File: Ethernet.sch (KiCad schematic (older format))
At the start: 11 parts

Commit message: Up
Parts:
- added U?: 93LC46, symbol 93LC46
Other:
- moved on the sheet: C?, R?, U?, Y?

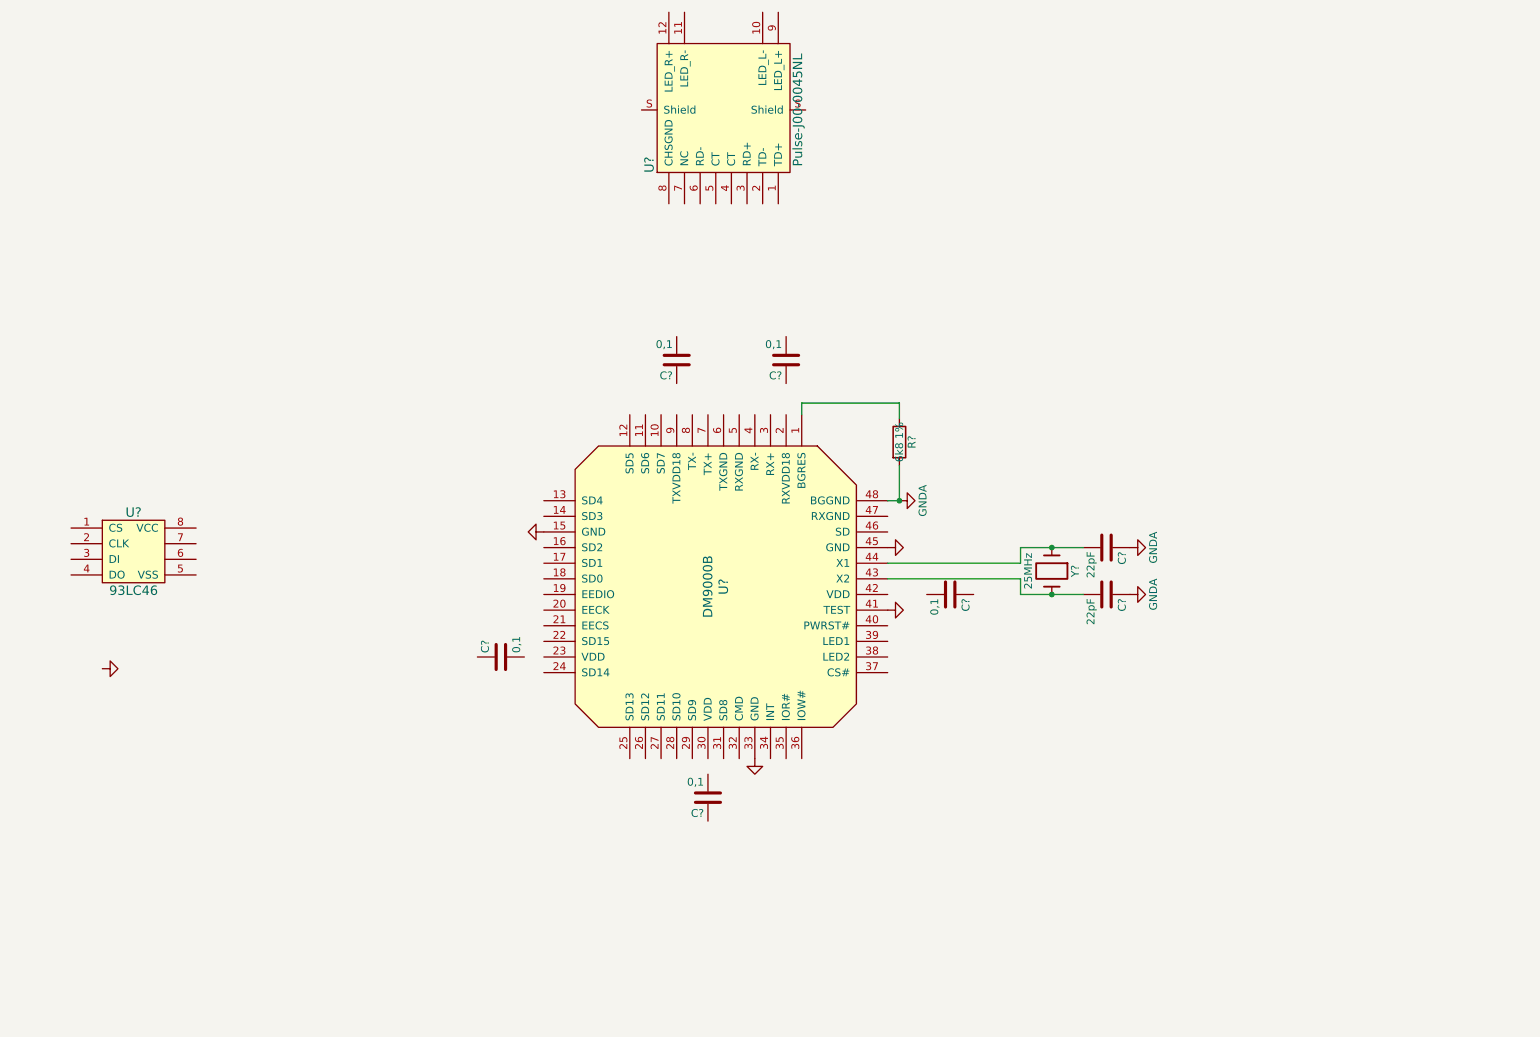
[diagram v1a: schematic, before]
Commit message: Pulse jack added
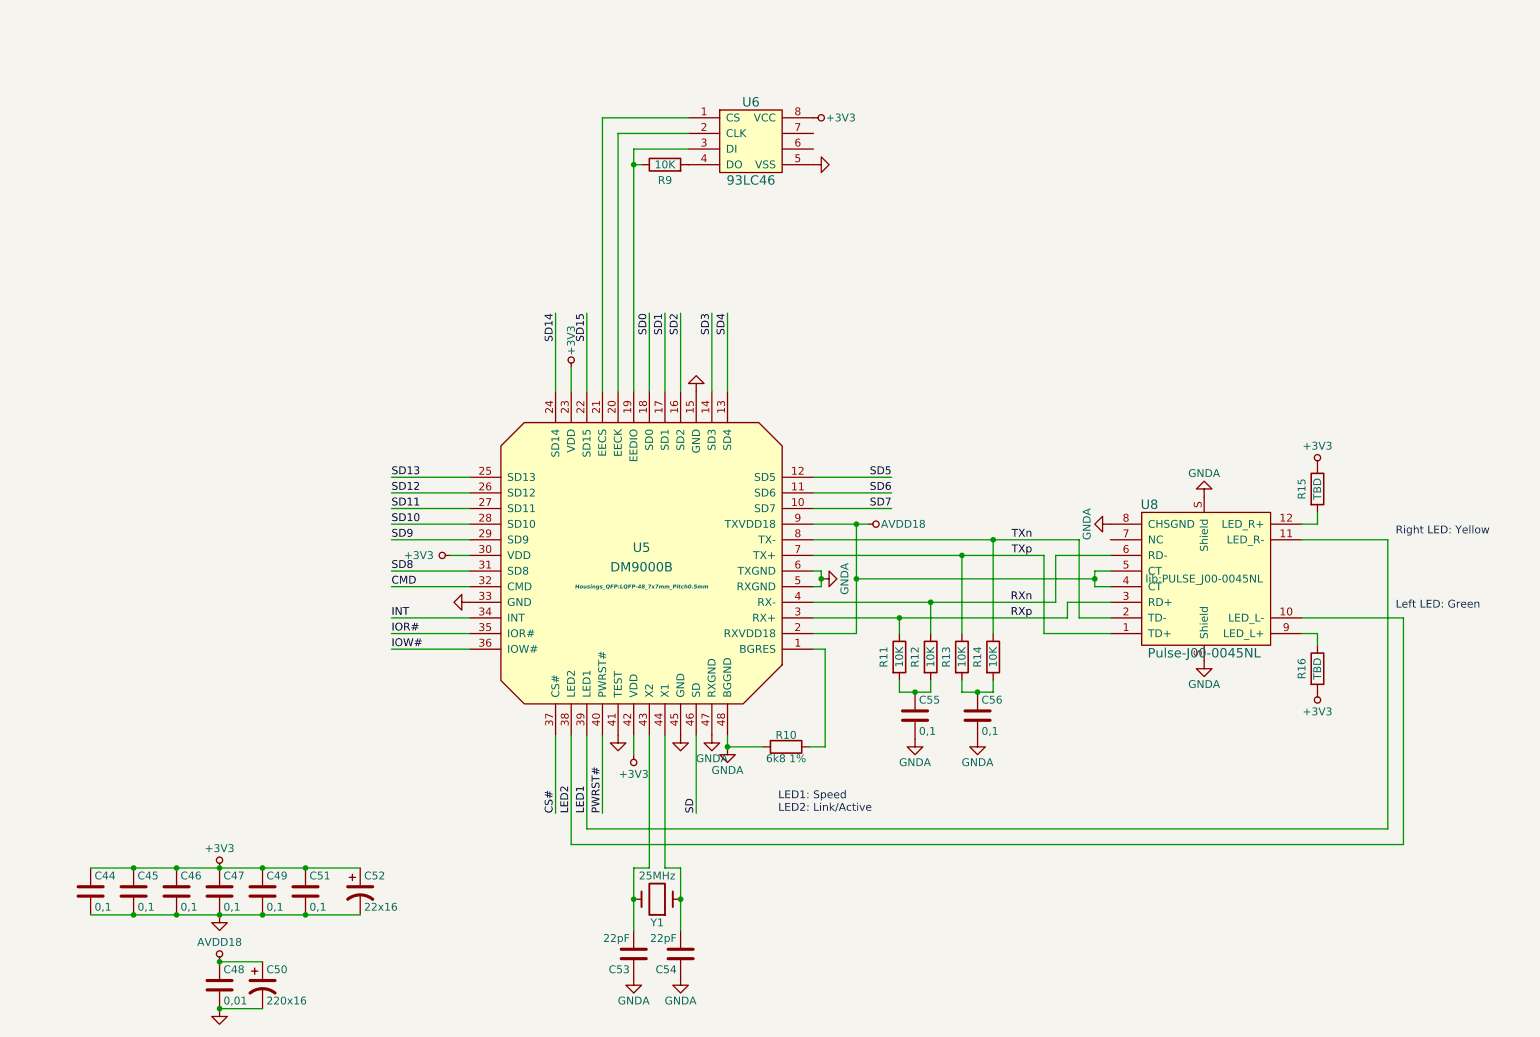
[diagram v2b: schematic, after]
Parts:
- added C44, C55, C56: 0,1, symbol C
- added C48: 0,01, symbol C
- added C50: 220x16, symbol CP1
- added C52: 22x16, symbol CP1
- added R11, R12, R13, R14, R9: 10K, symbol R
- added R15, R16: TBD, symbol R
- U5: renamed from U?; footprint (none) -> Housings_QFP:LQFP-48_7x7mm_Pitch0.5mm
- U8: renamed from U?; footprint (none) -> lib:PULSE_J00-0045NL
- gave numbers to parts that had none: 10
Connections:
- net GND: now also C45.2, C46.2, C47.2, C49.2, C51.2, U6.5 (VSS), C44.2, C48.2, C50.2, C52.2
- net GNDA: now also U5.47 (RXGND), U5.5 (RXGND), U5.6 (TXGND), U8.8 (CHSGND), U8.S (Shield), C55.2, C56.2
- net SD7: now reaches U5.10 (SD7)
- net SD6: now reaches U5.11 (SD6)
- net SD5: now reaches U5.12 (SD5)
- net SD4: now reaches U5.13 (SD4)
- net SD3: now reaches U5.14 (SD3)
- net SD2: now reaches U5.16 (SD2)
- net SD1: now reaches U5.17 (SD1)
- net SD0: now reaches U5.18 (SD0)
- net at U5.19 (EEDIO): now also U6.3 (DI), R9.1
- net AVDD18: now reaches U5.2 (RXVDD18)
- net AVDD18: now also U5.9 (TXVDD18), U8.4 (CT), U8.5 (CT), C48.1, C50.1
- net at U5.20 (EECK): now also U6.2 (CLK)
- net at U5.21 (EECS): now also U6.1 (CS)
- net SD15: now reaches U5.22 (SD15)
- net +3V3: now reaches U5.23 (VDD)
- net +3V3: now also C45.1, C46.1, C47.1, C49.1, C51.1, U5.30 (VDD), U5.42 (VDD), U6.8 (VCC), C44.1, C52.1, R15.1, R16.2
- net SD14: now reaches U5.24 (SD14)
- net SD13: now reaches U5.25 (SD13)
- net SD12: now reaches U5.26 (SD12)
- net SD11: now reaches U5.27 (SD11)
- net SD10: now reaches U5.28 (SD10)
- net SD9: now reaches U5.29 (SD9)
- net RXp: now reaches U5.3 (RX+)
- net RXp: now also U8.3 (RD+), R11.1
- net SD8: now reaches U5.31 (SD8)
- net CMD: now reaches U5.32 (CMD)
- net INT: now reaches U5.34 (INT)
- net IOR#: now reaches U5.35 (IOR#)
- net IOW#: now reaches U5.36 (IOW#)
- net CS#: now reaches U5.37 (CS#)
- net LED2: now reaches U5.38 (LED2)
- net LED2: now also U8.10 (LED_L-)
- net LED1: now reaches U5.39 (LED1)
- net LED1: now also U8.11 (LED_R-)
- net RXn: now reaches U5.4 (RX-)
- net RXn: now also U8.6 (RD-), R12.1
- net PWRST#: now reaches U5.40 (PWRST#)
- net SD: now reaches U5.46 (SD)
- net TXp: now reaches U5.7 (TX+)
- net TXp: now also U8.1 (TD+), R13.1
- net TXn: now reaches U5.8 (TX-)
- net TXn: now also U8.2 (TD-), R14.1
- net at U8.12 (LED_R+): now also R15.2
- net at U8.9 (LED_L+): now also R16.1
- net at U6.4 (DO): now also R9.2
- new net: C55.1, R11.2, R12.2
- new net: C56.1, R13.2, R14.2
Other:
- note added: "LED1: Speed\nLED2: Link/Active"
- note added: "Left LED: Green"
- note added: "Right LED: Yellow"
- moved on the sheet: C45, C46, C47, C49, C51, C53, C54, R10, U5, U6, U8, Y1

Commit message: Update
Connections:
- net SD: no longer names the net of U5.46 (SD)
- no-connect marks 0 -> 2
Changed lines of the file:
@@
 Wire Wire Line
 	6100 4125 6600 4125
-Text Label 4450 2875 3    50   ~ 0
+Text Label 2500 3050 2    50   ~ 0
 SD14
 Wire Wire Line
-	4450 3375 4450 2875
+	2000 3050 2500 3050
 Text Label 4650 2875 3    50   ~ 0
 SD15
@@
 Text Label 4750 6075 1    50   ~ 0
 PWRST#
-Wire Wire Line
-	5350 5575 5350 6075
-Text Label 5350 6075 1    50   ~ 0
-SD
 $Comp
 L GNDA #PWR0105
@@
 	-1   0    0    1
 $EndComp
+NoConn ~ 8000 4325
+Text HLabel 1775 1100 0    60   BiDi ~ 0
+ETH_SD[0:15]
+Wire Bus Line
+	1775 1100 1900 1100
+Wire Bus Line
+	1900 1100 1900 3050
+Text Label 2500 2950 2    50   ~ 0
+SD13
+Wire Wire Line
+	2000 2850 2500 2850
+Wire Wire Line
+	2000 2650 2500 2650
+Wire Wire Line
+	2000 2550 2500 2550
+Text Label 2500 2850 2    50   ~ 0
+SD12
+Text Label 2500 2750 2    50   ~ 0
+SD11
+Text Label 2500 2650 2    50   ~ 0
+SD10
+Text Label 2500 2550 2    50   ~ 0
+SD9
+Wire Wire Line
+	2000 2750 2500 2750
+Wire Wire Line
+	2000 2950 2500 2950
+Entry Wire Line
+	1900 1550 2000 1650
+Entry Wire Line
+	1900 1650 2000 1750
+Entry Wire Line
+	1900 1750 2000 1850
+Entry Wire Line
+	1900 1850 2000 1950
+Entry Wire Line
+	1900 1950 2000 2050
+Entry Wire Line
+	1900 2050 2000 2150
+Entry Wire Line
+	1900 2150 2000 2250
+Entry Wire Line
+	1900 2250 2000 2350
+Entry Wire Line
+	1900 2350 2000 2450
+Entry Wire Line
+	1900 2450 2000 2550
+Entry Wire Line
+	1900 2550 2000 2650
+Entry Wire Line
+	1900 2650 2000 2750
+Entry Wire Line
+	1900 2750 2000 2850
+Entry Wire Line
+	1900 2850 2000 2950
+Entry Wire Line
+	1900 2950 2000 3050
+Entry Wire Line
+	1900 3050 2000 3150
+Text Label 2500 1650 2    50   ~ 0
+SD0
+Wire Wire Line
+	2000 1650 2500 1650
+Text Label 2500 1750 2    50   ~ 0
+SD1
+Wire Wire Line
+	2000 1750 2500 1750
+Text Label 2500 1850 2    50   ~ 0
+SD2
+Wire Wire Line
+	2000 1850 2500 1850
+Text Label 2500 1950 2    50   ~ 0
+SD3
+Wire Wire Line
+	2000 1950 2500 1950
+Text Label 2500 2050 2    50   ~ 0
+SD4
+Wire Wire Line
+	2000 2050 2500 2050
+Text Label 2500 2350 2    50   ~ 0
+SD7
+Wire Wire Line
+	2000 2250 2500 2250
+Text Label 2500 2250 2    50   ~ 0
+SD6
+Text Label 2500 2150 2    50   ~ 0
+SD5
+Wire Wire Line
+	2000 2150 2500 2150
+Wire Wire Line
+	2000 2350 2500 2350
+Wire Wire Line
+	2000 2450 2500 2450
+Text Label 2500 2450 2    50   ~ 0
+SD8
+Text Label 2500 3150 2    50   ~ 0
+SD15
+Wire Wire Line
+	2000 3150 2500 3150
+Text Label 4450 2875 3    50   ~ 0
+SD14
+Wire Wire Line
+	4450 3375 4450 2875
+Wire Wire Line
+	1775 4000 2275 4000
+Text Label 2275 4000 2    50   ~ 0
+CMD
+Wire Wire Line
+	1775 4200 2275 4200
+Text Label 2275 4200 2    50   ~ 0
+INT
+Wire Wire Line
+	1775 4300 2275 4300
+Text Label 2275 4300 2    50   ~ 0
+IOR#
+Wire Wire Line
+	1775 4400 2275 4400
+Text Label 2275 4400 2    50   ~ 0
+IOW#
+Text Label 2275 4500 2    50   ~ 0
+CS#
+Text Label 2275 4600 2    50   ~ 0
+PWRST#
+Wire Wire Line
+	1775 4500 2275 4500
+Wire Wire Line
+	1775 4600 2275 4600
+Text HLabel 1775 4000 0    60   Input ~ 0
+CMD
+Text HLabel 1775 4200 0    60   Output ~ 0
+INT
+Text HLabel 1775 4300 0    60   Input ~ 0
+IOR#
+Text HLabel 1775 4400 0    60   Input ~ 0
+IOW#
+Text HLabel 1775 4500 0    60   Input ~ 0
+CS#
+Text HLabel 1775 4600 0    60   Input ~ 0
+PWRST#
+NoConn ~ 5350 5575
 $EndSCHEMATC

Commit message: Sch/pcb update
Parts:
- added R17: 000, symbol R
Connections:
- net GND: now also R17.2
- net GNDA: now also R17.1
- net SD0 renamed ETH_SD0
- net SD1 renamed ETH_SD1
- net SD10 renamed ETH_SD10
- net SD11 renamed ETH_SD11
- net SD12 renamed ETH_SD12
- net SD13 renamed ETH_SD13
- net SD14 renamed ETH_SD14
- net SD15 renamed ETH_SD15
- net SD2 renamed ETH_SD2
- net SD3 renamed ETH_SD3
- net SD4 renamed ETH_SD4
- net SD5 renamed ETH_SD5
- net SD6 renamed ETH_SD6
- net SD7 renamed ETH_SD7
- net SD8 renamed ETH_SD8
- net SD9 renamed ETH_SD9
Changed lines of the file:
@@
 	4950 5700 4950 5575
 Text Label 3400 3925 0    50   ~ 0
-SD13
+ETH_SD13
 Wire Wire Line
 	3900 4025 3400 4025
@@
 	3900 4525 3400 4525
 Text Label 3400 4025 0    50   ~ 0
-SD12
+ETH_SD12
 Text Label 3400 4125 0    50   ~ 0
-SD11
+ETH_SD11
 Text Label 3400 4225 0    50   ~ 0
-SD10
+ETH_SD10
 Text Label 3400 4325 0    50   ~ 0
-SD9
+ETH_SD9
 Text Label 3400 4525 0    50   ~ 0
-SD8
+ETH_SD8
 Wire Wire Line
 	6100 4225 6450 4225
@@
 Connection ~ 6150 4575
 Text Label 6600 4125 2    50   ~ 0
-SD7
+ETH_SD7
 Wire Wire Line
 	6100 4025 6600 4025
 Text Label 6600 4025 2    50   ~ 0
-SD6
+ETH_SD6
 Text Label 6600 3925 2    50   ~ 0
-SD5
+ETH_SD5
 Wire Wire Line
 	6100 3925 6600 3925
@@
 	6100 4125 6600 4125
 Text Label 2500 3050 2    50   ~ 0
-SD14
+ETH_SD14
 Wire Wire Line
 	2000 3050 2500 3050
 Text Label 4650 2875 3    50   ~ 0
-SD15
+ETH_SD15
 Wire Wire Line
 	4650 3375 4650 2875
 Text Label 5050 2875 3    50   ~ 0
-SD0
+ETH_SD0
 Wire Wire Line
 	5050 3375 5050 2875
 Text Label 5150 2875 3    50   ~ 0
-SD1
+ETH_SD1
 Wire Wire Line
 	5150 3375 5150 2875
 Text Label 5250 2875 3    50   ~ 0
-SD2
+ETH_SD2
 Wire Wire Line
 	5250 3375 5250 2875
 Text Label 5450 2875 3    50   ~ 0
-SD3
+ETH_SD3
 Wire Wire Line
 	5450 3375 5450 2875
 Text Label 5550 2875 3    50   ~ 0
-SD4
+ETH_SD4
 Wire Wire Line
 	5550 3375 5550 2875
@@
 	1900 1100 1900 3050
 Text Label 2500 2950 2    50   ~ 0
-SD13
+ETH_SD13
 Wire Wire Line
 	2000 2850 2500 2850
@@
 	2000 2550 2500 2550
 Text Label 2500 2850 2    50   ~ 0
-SD12
+ETH_SD12
 Text Label 2500 2750 2    50   ~ 0
-SD11
+ETH_SD11
 Text Label 2500 2650 2    50   ~ 0
-SD10
+ETH_SD10
 Text Label 2500 2550 2    50   ~ 0
-SD9
+ETH_SD9
 Wire Wire Line
 	2000 2750 2500 2750
@@
 	1900 3050 2000 3150
 Text Label 2500 1650 2    50   ~ 0
-SD0
+ETH_SD0
 Wire Wire Line
 	2000 1650 2500 1650
 Text Label 2500 1750 2    50   ~ 0
-SD1
+ETH_SD1
 Wire Wire Line
 	2000 1750 2500 1750
 Text Label 2500 1850 2    50   ~ 0
-SD2
+ETH_SD2
 Wire Wire Line
 	2000 1850 2500 1850
 Text Label 2500 1950 2    50   ~ 0
-SD3
+ETH_SD3
 Wire Wire Line
 	2000 1950 2500 1950
 Text Label 2500 2050 2    50   ~ 0
-SD4
+ETH_SD4
 Wire Wire Line
 	2000 2050 2500 2050
 Text Label 2500 2350 2    50   ~ 0
-SD7
+ETH_SD7
 Wire Wire Line
 	2000 2250 2500 2250
 Text Label 2500 2250 2    50   ~ 0
-SD6
+ETH_SD6
 Text Label 2500 2150 2    50   ~ 0
-SD5
+ETH_SD5
 Wire Wire Line
 	2000 2150 2500 2150
@@
 	2000 2450 2500 2450
 Text Label 2500 2450 2    50   ~ 0
-SD8
+ETH_SD8
 Text Label 2500 3150 2    50   ~ 0
-SD15
+ETH_SD15
 Wire Wire Line
 	2000 3150 2500 3150
 Text Label 4450 2875 3    50   ~ 0
-SD14
+ETH_SD14
 Wire Wire Line
 	4450 3375 4450 2875
@@
 PWRST#
 NoConn ~ 5350 5575
+$Comp
+L GND #PWR0114
+U 1 1 58165CEB
+P 6650 3025
+F 0 "#PWR0114" H 6650 2775 50  0001 C CNN
+F 1 "GND" H 6650 2875 50  0001 C CNN
+F 2 "" H 6650 3025 50  0000 C CNN
+F 3 "" H 6650 3025 50  0000 C CNN
+	1    6650 3025
+	1    0    0    -1
+$EndComp
+$Comp
+L GNDA #PWR0115
+U 1 1 58165E98
+P 7050 3025
+F 0 "#PWR0115" H 7050 2775 50  0001 C CNN
+F 1 "GNDA" H 7050 2875 50  0000 C CNN
+F 2 "" H 7050 3025 50  0000 C CNN
+F 3 "" H 7050 3025 50  0000 C CNN
+	1    7050 3025
+	1    0    0    -1
+$EndComp
+$Comp
+L R R17
+U 1 1 58165F7B
+P 6850 2925
+F 0 "R17" V 6750 2925 50  0000 C CNN
+F 1 "000" V 6850 2925 50  0000 C CNN
+F 2 "" V 6780 2925 50  0000 C CNN
+F 3 "" H 6850 2925 50  0000 C CNN
+	1    6850 2925
+	0    1    1    0
+$EndComp
+Wire Wire Line
+	6700 2925 6650 2925
+Wire Wire Line
+	6650 2925 6650 3025
+Wire Wire Line
+	7050 3025 7050 2925
+Wire Wire Line
+	7050 2925 7000 2925
 $EndSCHEMATC
